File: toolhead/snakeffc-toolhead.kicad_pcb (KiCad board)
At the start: 2 copper layers, 24.8 x 41.3 mm, 17 parts, among them J10 ZMIN, J11 SERVO, J12 E_STEPPER, J13 Conn_01x01, J14 Conn_01x01, J4 Conn_01x26, J5 HEATER_24V, J6 HEATER_SW, J7 THERMISTOR, J8 HOTEND_FAN, J9 PARTCOOLER_FAN, U2 ADXL345

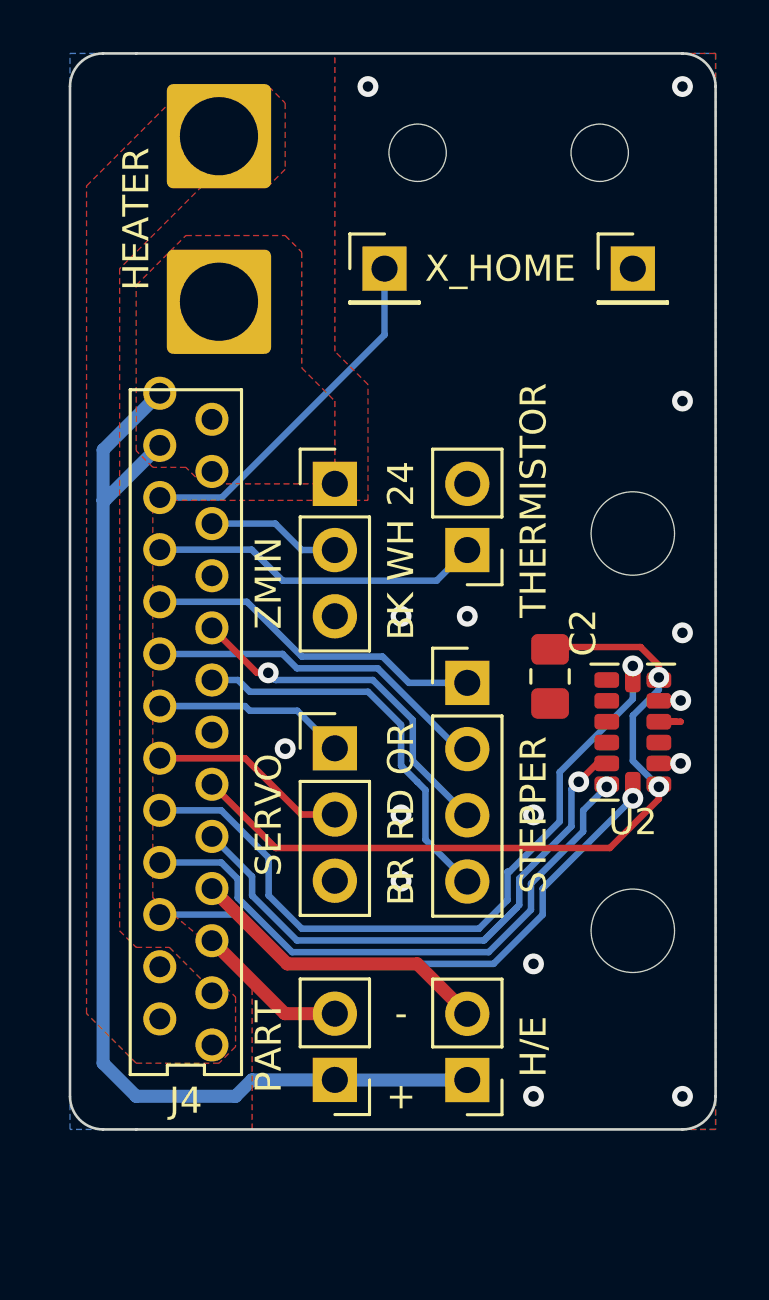
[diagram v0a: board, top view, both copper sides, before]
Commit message: gnd plane increased
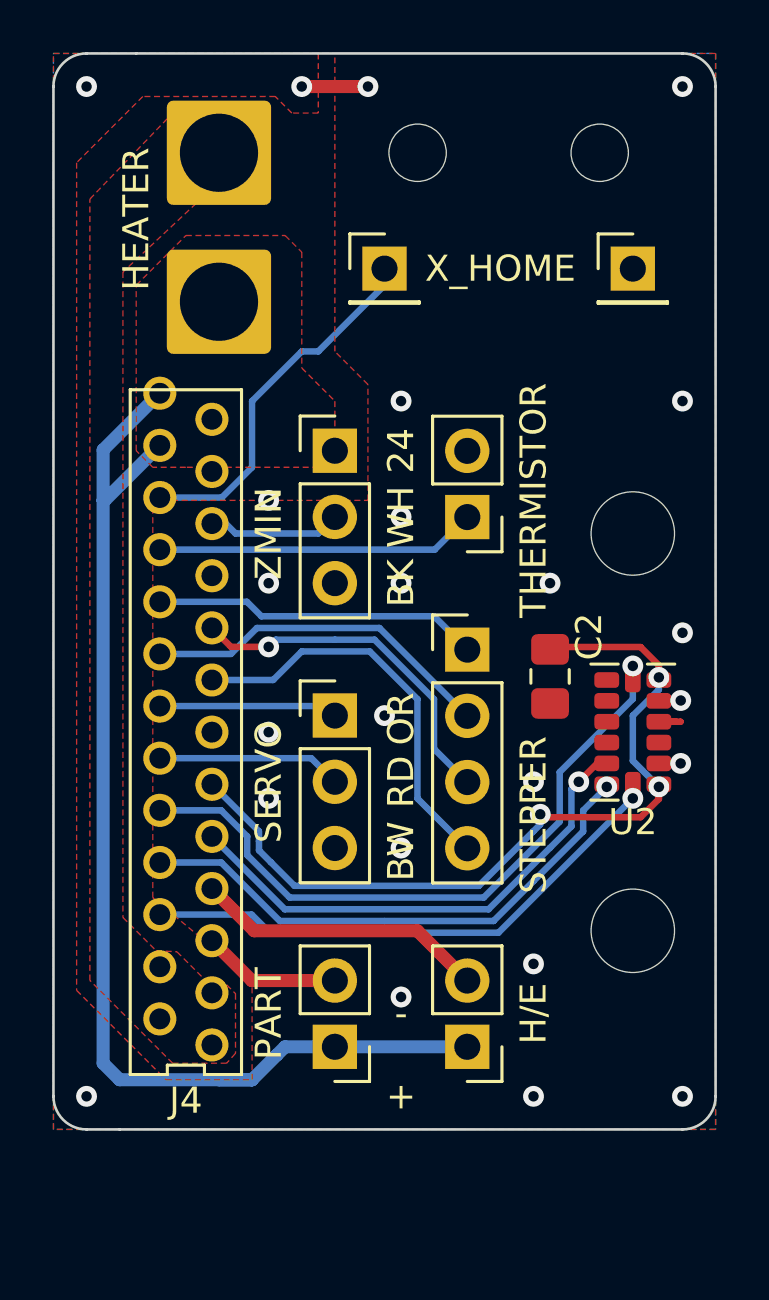
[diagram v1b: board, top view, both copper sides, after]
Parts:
- moved J12 1.28 mm to (209.6, 109.9)
- moved J8 1.28 mm to (209.6, 125.1)
- moved J9 1.27 mm to (204.5, 125.1)
- moved J10 1.27 mm to (204.5, 102.2)
- moved J7 1.27 mm to (209.6, 104.8)
- moved J11 1.26 mm to (204.5, 112.4)
- moved J6 0.64 mm to (200.0, 90.8)
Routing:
- net ADXL345_SDO: track 23.3 -> 19.5 mm
- net GND: track 3.17 -> 5.71 mm, vias 15 -> 24
- net +3V3: track 29.6 -> 32.0 mm, vias 2 -> 3
- net ADXL345_CS: track 27.5 -> 25.5 mm
- net ADXL345_SDA: track 22.7 -> 20.7 mm
- net ADXL345_SCL: track 22.2 -> 20.6 mm
- net +24V: track 44.4 -> 45.7 mm
- net STEPPER_B2: track 15.0 -> 15.6 mm
- net PART_FAN_SW: track 5.87 -> 5.35 mm
- net HOTEND_FAN_SW: track 11.8 -> 11.3 mm
- net STEPPER_A1: track 13.1 -> 12.6 mm
- net SERVO_BL_ORANGE: track 7.39 -> 6.87 mm
- net +5V: track 7.61 -> 7.09 mm
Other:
- board size 24.8 x 41.3 mm -> 25.4 x 41.3 mm
- board text added: "BW"
- board text removed: "BR"

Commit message: toolhead artwork
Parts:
- removed J14: Conn_01x01, Connector_PinHeader_2.54mm:PinHeader_1x01_P2.54mm_Vertical
- removed J6: HEATER_SW, Connector_Wire:SolderWire-2.5sqmm_1x01_D2.4mm_OD3.6mm
- removed J7: THERMISTOR, Connector_PinHeader_2.54mm:PinHeader_1x02_P2.54mm_Vertical
- added J1: PT100_NTC, Connector_PinHeader_2.54mm:PinHeader_1x04_P2.54mm_Vertical, F.Cu at (209.6, 110.0)
- added J16: AUX1, Connector_PinHeader_2.54mm:PinHeader_1x01_P2.54mm_Vertical, F.Cu at (203.2, 102.4)
- C2: footprint Capacitor_SMD:C_0805_2012Metric_Pad1.18x1.45mm_HandSolder -> Capacitor_SMD:C_0603_1608Metric
- J13: value Conn_01x01 -> X_HOME; footprint Connector_PinHeader_2.54mm:PinHeader_1x01_P2.54mm_Vertical -> ffc_connectors:limit_switch
- J4: value Conn_01x26 -> Conn_01x30; footprint FFCconnector:FFC26pinTH -> ffc_connectors:ffc-30pin
- J5: value HEATER_24V -> HEATER; footprint Connector_Wire:SolderWire-2.5sqmm_1x01_D2.4mm_OD3.6mm -> ffc_connectors:KF301-5.0
- moved J5 6.47 mm to (199.0, 90.1)
- moved J11 5.36 mm to (203.2, 117.6)
- moved J10 5.36 mm to (203.2, 107.4)
- moved J9 5.36 mm to (203.2, 130.3)
- moved J12 5.20 mm to (209.6, 115.1)
- moved J8 5.20 mm to (209.6, 130.3)
- moved J13 4.76 mm to (211.1, 95.2)
- moved C2 4.28 mm to (216.9, 110.0), turned to 0 degrees
- moved J4 0.94 mm to (198.8, 114.0), turned to -90 degrees
- moved U2 0.51 mm to (215.9, 113.5)
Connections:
- J10 pad 2: PROBE_ZMIN_BL_WHITE -> PROBE_ZMIN_24V
- J11 pad 1: SERVO_BL_ORANGE -> SERVO_NEOPIXEL
- J4 pad 1: HEATER_SW -> +24V
- J4 pad 10: ADXL345_CS -> PROBE_ZMIN_24V
- J4 pad 11: +3V3 -> GND
- J4 pad 12: +5V -> GND
- J4 pad 13: GND -> SERVO_NEOPIXEL
- J4 pad 14: SERVO_BL_ORANGE -> STEPPER_A1
- J4 pad 15: STEPPER_B2 -> STEPPER_B1
- J4 pad 17: STEPPER_B1 -> STEPPER_B2
- J4 pad 18: STEPPER_A1 -> ADXL345_SCL
- J4 pad 19: GND -> +3V3
- J4 pad 2: HEATER_SW -> +24V
- J4 pad 20: THERM -> +5V
- J4 pad 21: PROBE_ZMIN_BL_WHITE -> +5V
- J4 pad 22: X_HOME -> ADXL345_CS
- J4 pad 23: +24V -> ADXL345_SDO
- J4 pad 24: +24V -> HOTEND_FAN_SW
- J4 pad 25: +24V -> ADXL345_SDA
- J4 pad 26: +24V -> PART_FAN_SW
- J4 pad 3: HEATER_SW -> +24V
- J4 pad 4: HEATER_SW -> +24V
- J4 pad 5: PART_FAN_SW -> X_HOME
- J4 pad 6: ADXL345_SCL -> THERM_AUX_2
- J4 pad 7: HOTEND_FAN_SW -> THERM_AUX_1
- J4 pad 8: ADXL345_SDA -> THERM_0
- J4 pad 9: ADXL345_SDO -> GNDA
- J5 pad 1: +24V -> HEATER_SW
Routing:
- net HEATER_SW: track 0.00 -> 47.4 mm
- net +24V: track 45.7 -> 69.4 mm, vias 0 -> 1
- net THERM_AUX_1: track 0.00 -> 17.6 mm
- net GNDA: track 0.00 -> 16.8 mm
- net THERM_AUX_2: track 0.00 -> 14.5 mm
- net THERM_0: track 0.00 -> 12.6 mm
- net THERM: track 12.3 -> 0.00 mm
- net ADXL345_SCL: track 20.6 -> 31.8 mm, vias 1 -> 2
- net SERVO_NEOPIXEL: track 0.00 -> 9.85 mm, vias 0 -> 1
- net ADXL345_SDO: track 19.5 -> 26.5 mm, vias 1 -> 0
- net SERVO_BL_ORANGE: track 6.87 -> 0.00 mm
- net ADXL345_SDA: track 20.7 -> 26.2 mm
- net PROBE_ZMIN_BL_WHITE: track 5.14 -> 0.00 mm
- net STEPPER_B1: track 13.6 -> 18.1 mm, vias 1 -> 0
- net PROBE_ZMIN_24V: track 0.00 -> 3.87 mm
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- removed copper zone on F.Cu, net +24V
- removed copper zone on F.Cu, net HEATER_SW
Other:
- board size 25.4 x 41.3 mm -> 25.4 x 45.2 mm
- board text added: "FFC Toolhead r3"
- board text removed: "+"
- board text removed: "-"
- board text removed: "24"
- board text removed: "BK"
- board text removed: "BW"
- board text removed: "H/E"
- board text removed: "HEATER"
- board text removed: "OR"
- board text removed: "PART"
- board text removed: "RD"
- board text removed: "SERVO"
- board text removed: "STEPPER"
- board text removed: "THERMISTOR"
- board text removed: "WH"
- board text removed: "X_HOME"
- board text removed: "ZMIN"

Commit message: r3 jlcpcb
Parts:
- added REF**: MountingHole_3.2mm_M3, MountingHole:MountingHole_3.2mm_M3, F.Cu at (215.9, 129.0)
- moved J5 1.30 mm to (199.5, 91.3)
- moved C2 1.27 mm to (215.6, 110.0)
- moved U2 0.51 mm to (215.4, 113.5)
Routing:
- net X_HOME: track 15.7 -> 18.4 mm
- net HEATER_SW: track 47.4 -> 46.0 mm
- net +24V: track 69.4 -> 68.4 mm
- net +3V3: track 30.6 -> 29.7 mm
- net ADXL345_SDA: track 26.2 -> 25.7 mm
- net ADXL345_SCL: track 31.8 -> 31.3 mm
- net ADXL345_CS: track 23.2 -> 22.7 mm
- net GND: vias 27 -> 23
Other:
- board size 25.4 x 45.2 mm -> 23.7 x 45.2 mm
